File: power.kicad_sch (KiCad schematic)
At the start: 5 parts, among them J1 Screw_Terminal_01x02

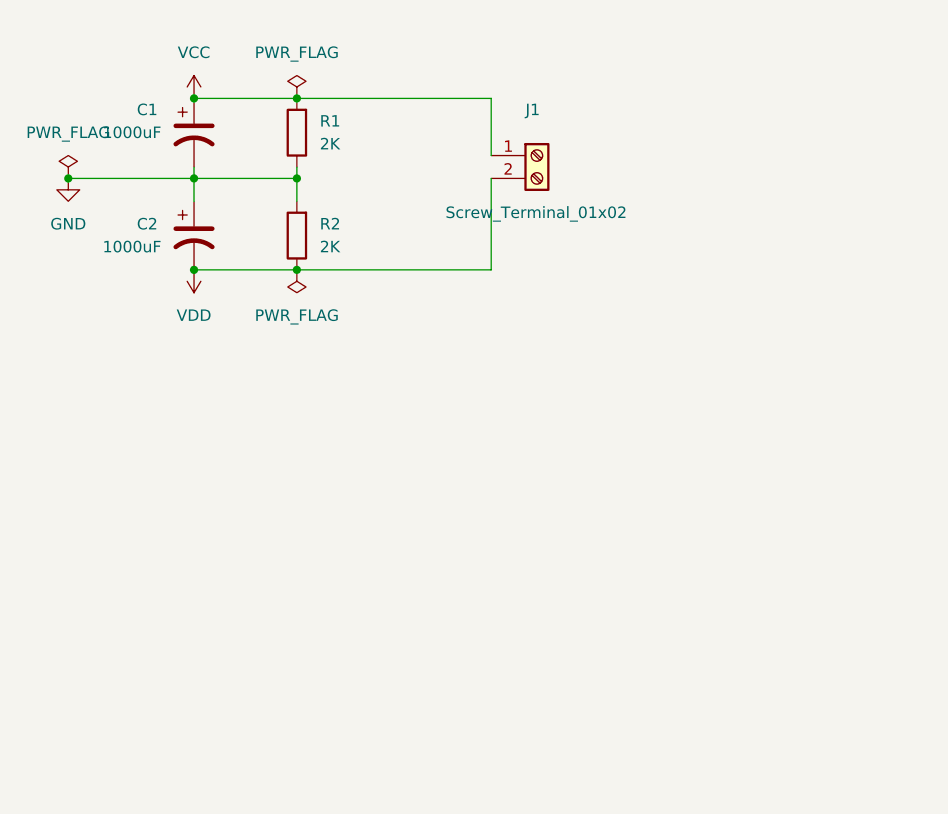
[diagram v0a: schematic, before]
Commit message: Added decoupling and output caps
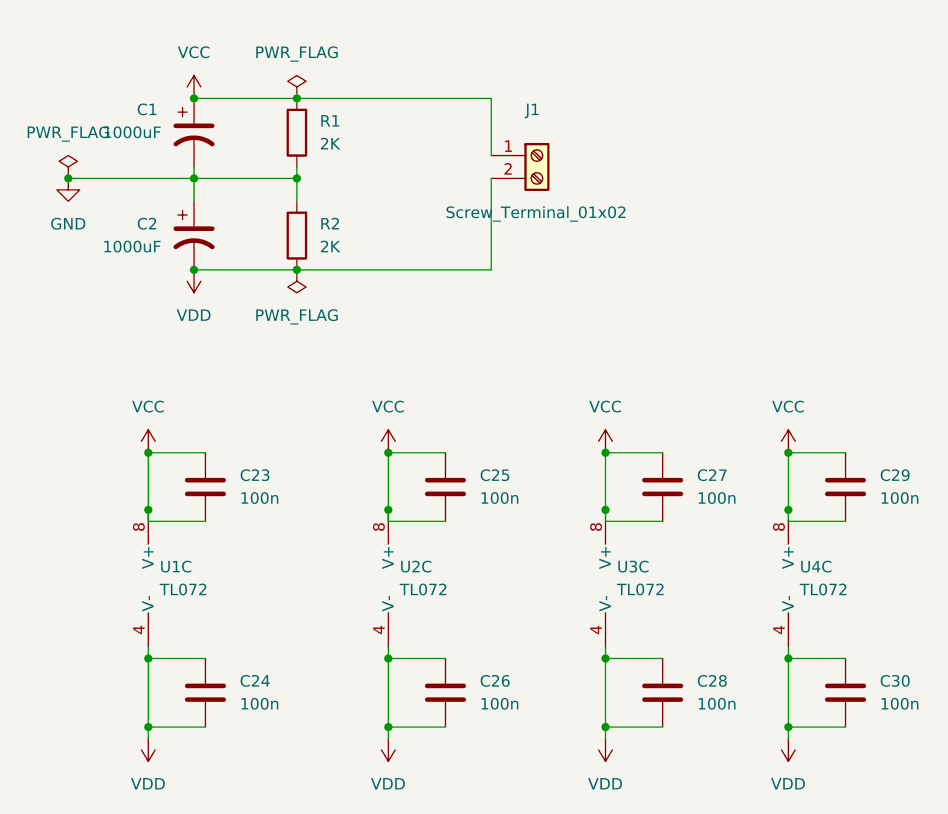
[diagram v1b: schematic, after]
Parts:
- added C23, C24, C25, C26, C27, C28, C29, C30: 100n, symbol Device:C
- added U1, U2, U3, U4: TL072, symbol Amplifier_Operational:TL072
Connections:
- net VCC: now also C23.1, C23.2, C25.1, C25.2, C27.1, C27.2, C29.1, C29.2, U1.8 (V+), U2.8 (V+), U3.8 (V+), U4.8 (V+)
- net VDD: now also C24.1, C24.2, C26.1, C26.2, C28.1, C28.2, C30.1, C30.2, U1.4 (V-), U2.4 (V-), U3.4 (V-), U4.4 (V-)

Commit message: Refactored and made modular inputs
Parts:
- added J5: Power Input 5v, symbol Connector:Screw_Terminal_01x02
- J4: renamed from J1; value Screw_Terminal_01x02 -> Power Input 24V
- renumbered C30 to C10, C23 to C3, C24 to C4, C25 to C5, C26 to C6, C27 to C7, C28 to C8, C29 to C9
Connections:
- new net +5V: J5.1 (Pin_1)
- new net GND2: J5.2 (Pin_2)

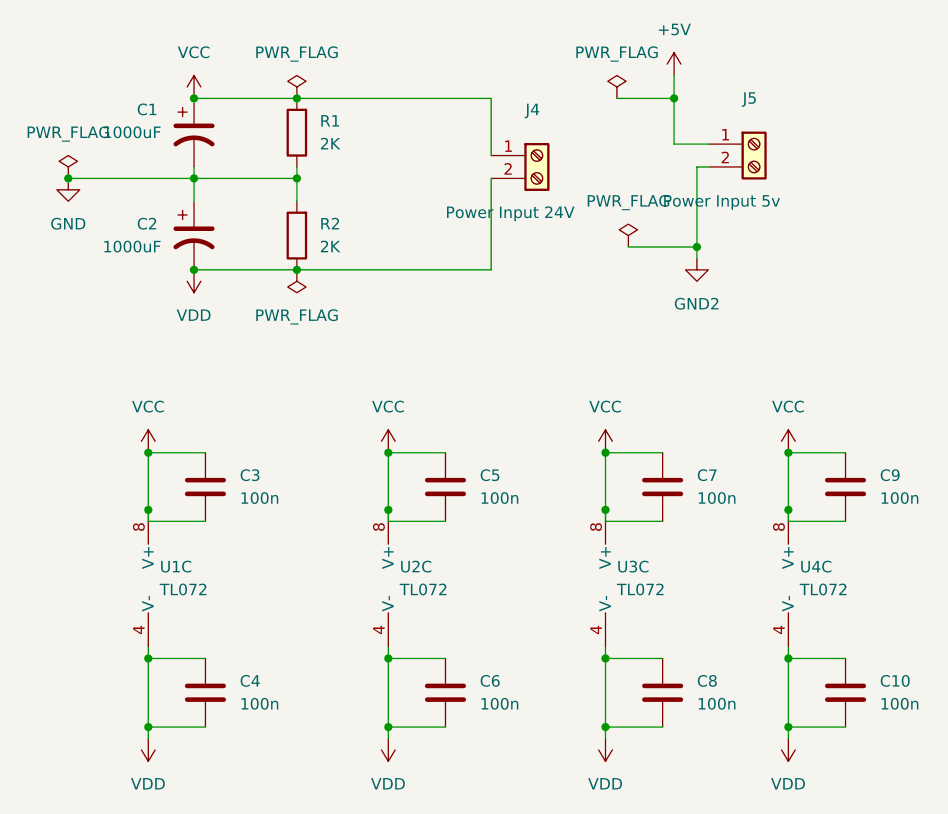
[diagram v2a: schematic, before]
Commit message: Update footprints
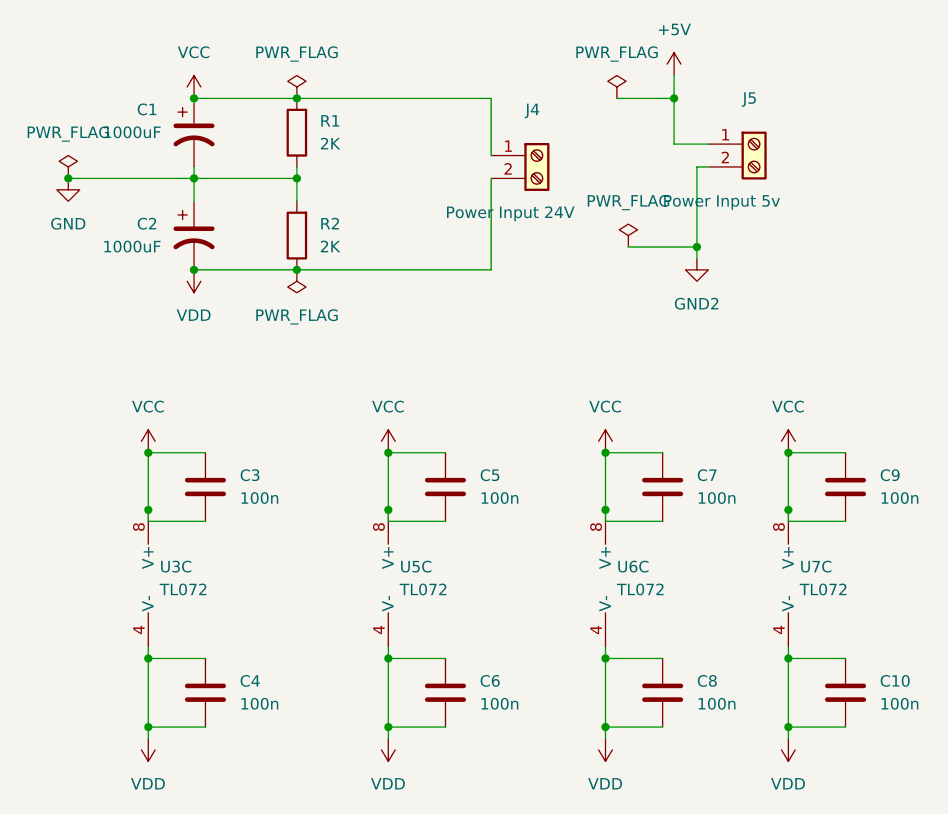
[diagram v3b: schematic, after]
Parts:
- C1, C2: footprint (none) -> Capacitor_THT:CP_Radial_D10.0mm_P5.00mm
- C10, C3, C4, C5, C6, C7, C8, C9: footprint (none) -> Capacitor_THT:C_Rect_L10.3mm_W4.5mm_P7.50mm_MKS4
- J4, J5: footprint (none) -> TerminalBlock:TerminalBlock_bornier-2_P5.08mm
- U3: renamed from U1; footprint (none) -> Package_DIP:DIP-8_W7.62mm_Socket
- U5: renamed from U2; footprint (none) -> Package_DIP:DIP-8_W7.62mm_Socket
- U6: renamed from U3; footprint (none) -> Package_DIP:DIP-8_W7.62mm_Socket
- U7: renamed from U4; footprint (none) -> Package_DIP:DIP-8_W7.62mm_Socket
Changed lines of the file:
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@@
   (symbol (lib_id "Amplifier_Operational:TL072") (at 127 95.25 0) (unit 3)
     (in_bom yes) (on_board yes) (fields_autoplaced)
-    (property "Reference" "U3" (id 0) (at 125.73 93.9799 0)
+    (property "Reference" "U6" (id 0) (at 125.73 93.9799 0)
       (effects (font (size 1.27 1.27)) (justify left))
     )
@@
       (effects (font (size 1.27 1.27)) (justify left))
     )
-    (property "Footprint" "" (id 2) (at 127 95.25 0)
+    (property "Footprint" "Package_DIP:DIP-8_W7.62mm_Socket" (id 2) (at 127 95.25 0)
       (effects (font (size 1.27 1.27)) hide)
     )
@@
       (effects (font (size 1.27 1.27)) (justify left))
     )
-    (property "Footprint" "" (id 2) (at 116.84 48.26 0)
+    (property "Footprint" "TerminalBlock:TerminalBlock_bornier-2_P5.08mm" (id 2) (at 116.84 48.26 0)
       (effects (font (size 1.27 1.27)) hide)
     )
@@
       (effects (font (size 1.27 1.27)) (justify left))
     )
-    (property "Footprint" "" (id 2) (at 107.6452 111.76 0)
+    (property "Footprint" "Capacitor_THT:C_Rect_L10.3mm_W4.5mm_P7.50mm_MKS4" (id 2) (at 107.6452 111.76 0)
       (effects (font (size 1.27 1.27)) hide)
     )
@@
   (symbol (lib_id "power:PWR_FLAG") (at 127 58.42 0) (unit 1)
     (in_bom yes) (on_board yes) (fields_autoplaced)
-    (property "Reference" "#FLG?" (id 0) (at 127 56.515 0)
+    (property "Reference" "#FLG0101" (id 0) (at 127 56.515 0)
       (effects (font (size 1.27 1.27)) hide)
     )
@@
       (effects (font (size 1.27 1.27)) (justify left))
     )
-    (property "Footprint" "" (id 2) (at 80.9752 111.76 0)
+    (property "Footprint" "Capacitor_THT:C_Rect_L10.3mm_W4.5mm_P7.50mm_MKS4" (id 2) (at 80.9752 111.76 0)
       (effects (font (size 1.27 1.27)) hide)
     )
@@
       (effects (font (size 1.27 1.27)) (justify left))
     )
-    (property "Footprint" "" (id 2) (at 131.7752 111.76 0)
+    (property "Footprint" "Capacitor_THT:C_Rect_L10.3mm_W4.5mm_P7.50mm_MKS4" (id 2) (at 131.7752 111.76 0)
       (effects (font (size 1.27 1.27)) hide)
     )
@@
       (effects (font (size 1.27 1.27)) (justify left))
     )
-    (property "Footprint" "" (id 2) (at 80.9752 88.9 0)
+    (property "Footprint" "Capacitor_THT:C_Rect_L10.3mm_W4.5mm_P7.50mm_MKS4" (id 2) (at 80.9752 88.9 0)
       (effects (font (size 1.27 1.27)) hide)
     )
@@
       (effects (font (size 1.27 1.27)) (justify left))
     )
-    (property "Footprint" "" (id 2) (at 152.0952 111.76 0)
+    (property "Footprint" "Capacitor_THT:C_Rect_L10.3mm_W4.5mm_P7.50mm_MKS4" (id 2) (at 152.0952 111.76 0)
       (effects (font (size 1.27 1.27)) hide)
     )
@@
   (symbol (lib_id "power:PWR_FLAG") (at 125.73 41.91 0) (unit 1)
     (in_bom yes) (on_board yes) (fields_autoplaced)
-    (property "Reference" "#FLG?" (id 0) (at 125.73 40.005 0)
+    (property "Reference" "#FLG0102" (id 0) (at 125.73 40.005 0)
       (effects (font (size 1.27 1.27)) hide)
     )
@@
       (effects (font (size 1.27 1.27)) (justify left))
     )
-    (property "Footprint" "" (id 2) (at 152.0952 88.9 0)
+    (property "Footprint" "Capacitor_THT:C_Rect_L10.3mm_W4.5mm_P7.50mm_MKS4" (id 2) (at 152.0952 88.9 0)
       (effects (font (size 1.27 1.27)) hide)
     )
@@
       (effects (font (size 1.27 1.27)) (justify left))
     )
-    (property "Footprint" "" (id 2) (at 78.74 57.15 0)
+    (property "Footprint" "Capacitor_THT:CP_Radial_D10.0mm_P5.00mm" (id 2) (at 78.74 57.15 0)
       (effects (font (size 1.27 1.27)) hide)
     )
@@
       (effects (font (size 1.27 1.27)) (justify left))
     )
-    (property "Footprint" "" (id 2) (at 140.97 46.99 0)
+    (property "Footprint" "TerminalBlock:TerminalBlock_bornier-2_P5.08mm" (id 2) (at 140.97 46.99 0)
       (effects (font (size 1.27 1.27)) hide)
     )
@@
   (symbol (lib_id "Amplifier_Operational:TL072") (at 102.87 95.25 0) (unit 3)
     (in_bom yes) (on_board yes) (fields_autoplaced)
-    (property "Reference" "U2" (id 0) (at 101.6 93.9799 0)
+    (property "Reference" "U5" (id 0) (at 101.6 93.9799 0)
       (effects (font (size 1.27 1.27)) (justify left))
     )
@@
       (effects (font (size 1.27 1.27)) (justify left))
     )
-    (property "Footprint" "" (id 2) (at 102.87 95.25 0)
+    (property "Footprint" "Package_DIP:DIP-8_W7.62mm_Socket" (id 2) (at 102.87 95.25 0)
       (effects (font (size 1.27 1.27)) hide)
     )
@@
       (effects (font (size 1.27 1.27)) (justify left))
     )
-    (property "Footprint" "" (id 2) (at 131.7752 88.9 0)
+    (property "Footprint" "Capacitor_THT:C_Rect_L10.3mm_W4.5mm_P7.50mm_MKS4" (id 2) (at 131.7752 88.9 0)
       (effects (font (size 1.27 1.27)) hide)
     )
@@
       (effects (font (size 1.27 1.27)) (justify left))
     )
-    (property "Footprint" "" (id 2) (at 78.74 45.72 0)
+    (property "Footprint" "Capacitor_THT:CP_Radial_D10.0mm_P5.00mm" (id 2) (at 78.74 45.72 0)
       (effects (font (size 1.27 1.27)) hide)
     )
@@
   (symbol (lib_id "Amplifier_Operational:TL072") (at 76.2 95.25 0) (unit 3)
     (in_bom yes) (on_board yes) (fields_autoplaced)
-    (property "Reference" "U1" (id 0) (at 74.93 93.9799 0)
+    (property "Reference" "U3" (id 0) (at 74.93 93.9799 0)
       (effects (font (size 1.27 1.27)) (justify left))
     )
@@
       (effects (font (size 1.27 1.27)) (justify left))
     )
-    (property "Footprint" "" (id 2) (at 76.2 95.25 0)
+    (property "Footprint" "Package_DIP:DIP-8_W7.62mm_Socket" (id 2) (at 76.2 95.25 0)
       (effects (font (size 1.27 1.27)) hide)
     )
@@
       (effects (font (size 1.27 1.27)) (justify left))
     )
-    (property "Footprint" "" (id 2) (at 107.6452 88.9 0)
+    (property "Footprint" "Capacitor_THT:C_Rect_L10.3mm_W4.5mm_P7.50mm_MKS4" (id 2) (at 107.6452 88.9 0)
       (effects (font (size 1.27 1.27)) hide)
     )
@@
   (symbol (lib_id "Amplifier_Operational:TL072") (at 147.32 95.25 0) (unit 3)
     (in_bom yes) (on_board yes) (fields_autoplaced)
-    (property "Reference" "U4" (id 0) (at 146.05 93.9799 0)
+    (property "Reference" "U7" (id 0) (at 146.05 93.9799 0)
       (effects (font (size 1.27 1.27)) (justify left))
     )
@@
       (effects (font (size 1.27 1.27)) (justify left))
     )
-    (property "Footprint" "" (id 2) (at 147.32 95.25 0)
-      (effects (font (size 1.27 1.27)) hide)
-    )
+    (property "Footprint" "Package_DIP:DIP-8_W7.62mm_Socket" (id 2) (at 147.32 95.25 0)
+      (effects (font (size 1.27 1.27)) hide)
+    )

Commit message: Finalize schematic and start with PCB layout
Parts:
- R1, R2: value 2K -> 10K; footprint (none) -> Resistor_THT:R_Axial_DIN0207_L6.3mm_D2.5mm_P10.16mm_Horizontal
- renumbered U3 to U1, U5 to U2, U6 to U3, U7 to U4
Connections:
- net GND: now also C10.2, C3.2, C4.2, C5.2, C6.2, C7.2, C8.2, C9.2
- net VCC: no longer C3.2, C5.2, C7.2, C9.2
- net VDD: no longer C10.2, C4.2, C6.2, C8.2
